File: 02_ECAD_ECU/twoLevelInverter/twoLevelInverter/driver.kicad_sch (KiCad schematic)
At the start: 30 parts, among them IC2 INA240A4DR, IC3 BTN8982TAAUMA1, IC4 INA240A4DR, IC5 BTN8982TAAUMA1, IC6 INA240A4DR, IC7 BTN8982TAAUMA1

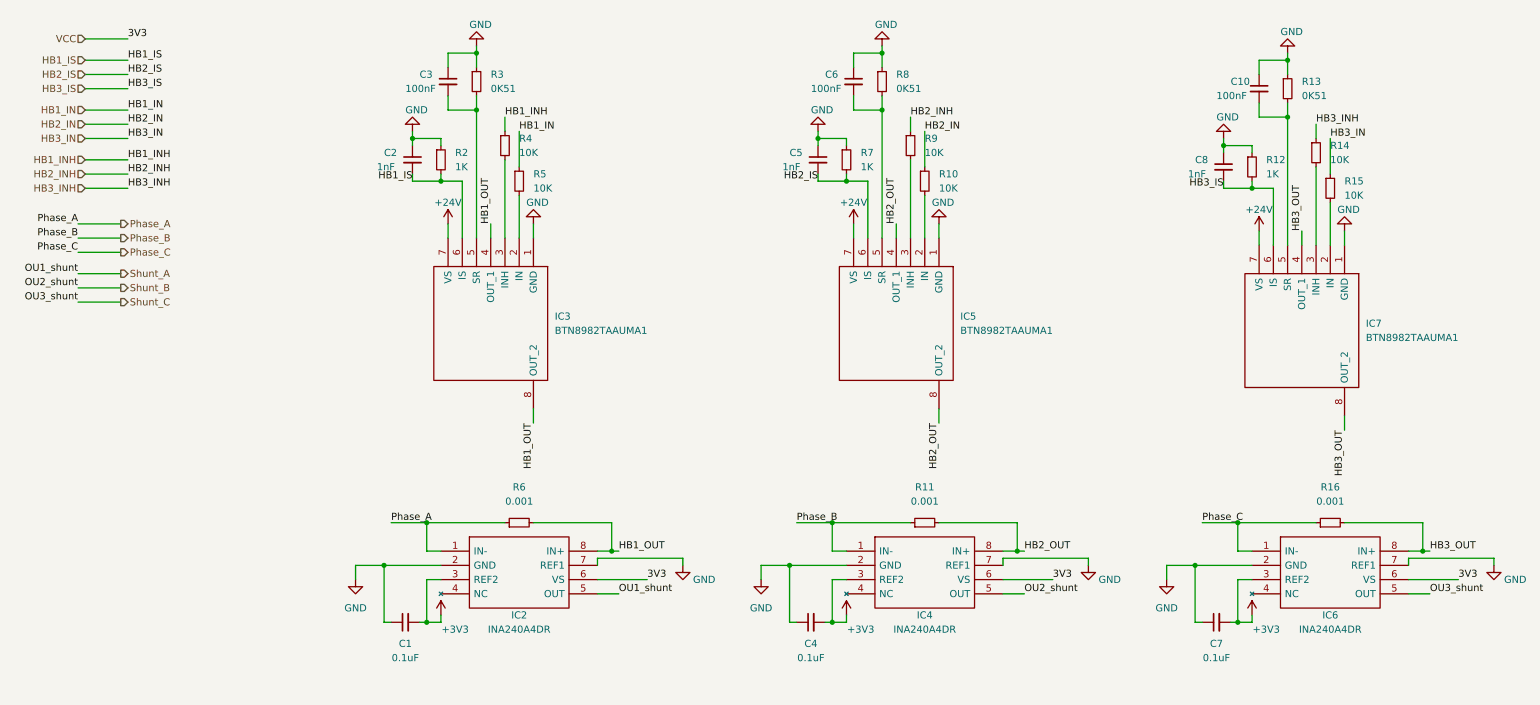
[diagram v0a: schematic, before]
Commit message: encoder, pwm, hall signals mapped
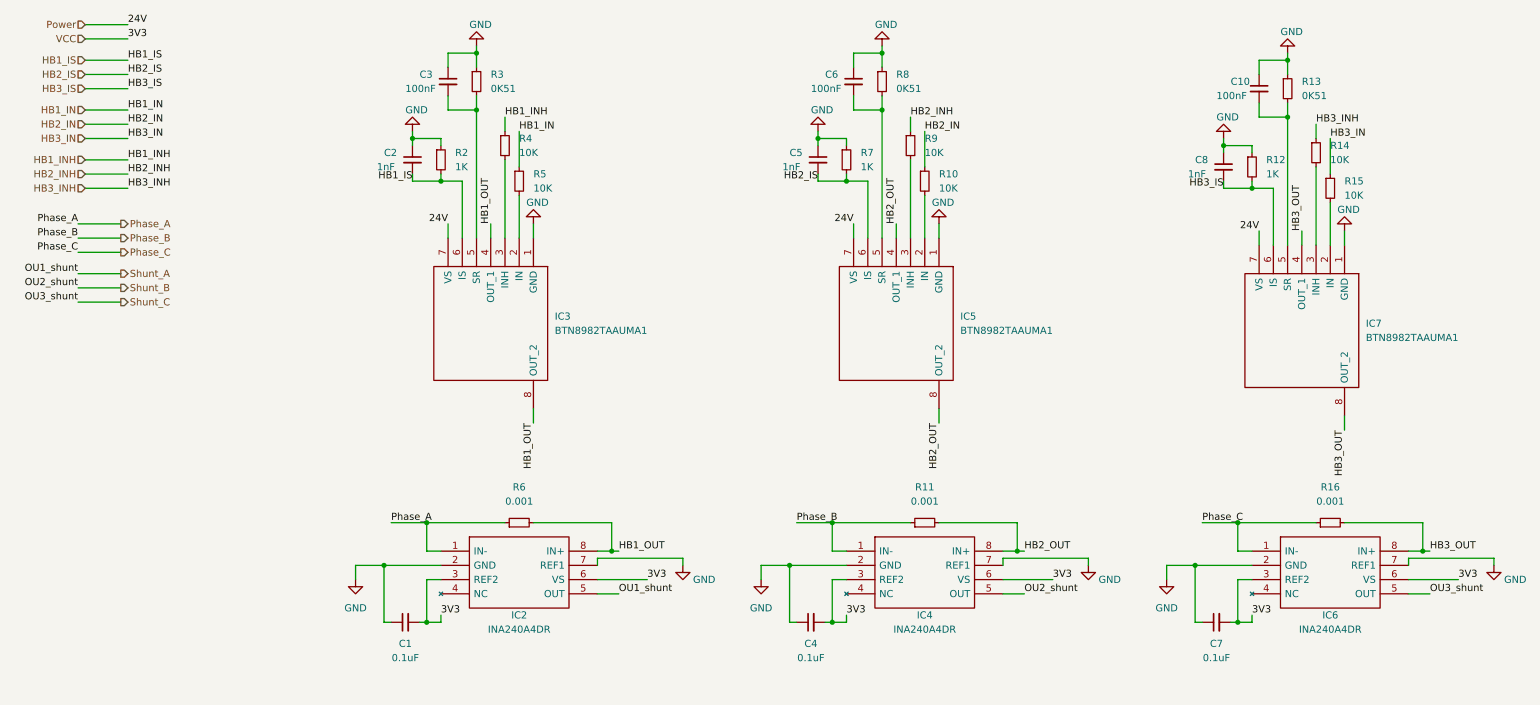
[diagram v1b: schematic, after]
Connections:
- net +3V3 is gone; now on net VCC: C1.2, C4.2, C7.2, IC2.3 (REF2), IC4.3 (REF2), IC6.3 (REF2)
- net +24V renamed Power
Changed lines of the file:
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@@
+    (stroke (width 0) (type default) (color 0 0 0 0))
+  )
+  (wire (pts (xy 25.4 17.78) (xy 33.02 17.78))
     (stroke (width 0) (type default) (color 0 0 0 0))
   )
@@
     (effects (font (size 1.27 1.27)) (justify left bottom))
   )
+  (label "24V" (at 234.95 54.61 180)
+    (effects (font (size 1.27 1.27)) (justify right bottom))
+  )
   (label "Phase_B" (at 152.4 106.68 0)
     (effects (font (size 1.27 1.27)) (justify left bottom))
@@
     (effects (font (size 1.27 1.27)) (justify left bottom))
   )
+  (label "3V3" (at 161.29 123.19 0)
+    (effects (font (size 1.27 1.27)) (justify left bottom))
+  )
   (label "HB2_OUT" (at 170.18 53.34 90)
     (effects (font (size 1.27 1.27)) (justify left bottom))
@@
     (effects (font (size 1.27 1.27)) (justify left bottom))
   )
+  (label "24V" (at 162.56 53.34 180)
+    (effects (font (size 1.27 1.27)) (justify right bottom))
+  )
   (label "HB1_IN" (at 102.87 36.83 0)
     (effects (font (size 1.27 1.27)) (justify left bottom))
   )
+  (label "24V" (at 90.17 53.34 180)
+    (effects (font (size 1.27 1.27)) (justify right bottom))
+  )
   (label "Phase_A" (at 80.01 106.68 0)
     (effects (font (size 1.27 1.27)) (justify left bottom))
@@
     (effects (font (size 1.27 1.27)) (justify left bottom))
   )
+  (label "3V3" (at 88.9 123.19 0)
+    (effects (font (size 1.27 1.27)) (justify left bottom))
+  )
+  (label "3V3" (at 233.68 123.19 0)
+    (effects (font (size 1.27 1.27)) (justify left bottom))
+  )
   (label "HB2_IS" (at 156.21 45.72 180)
     (effects (font (size 1.27 1.27)) (justify right bottom))
@@
   (label "HB1_IS" (at 83.82 45.72 180)
     (effects (font (size 1.27 1.27)) (justify right bottom))
+  )
+  (label "24V" (at 33.02 17.78 0)
+    (effects (font (size 1.27 1.27)) (justify left bottom))
   )
   (label "3V3" (at 270.51 116.84 0)
@@
   )
   (hierarchical_label "VCC" (shape input) (at 25.4 20.32 180)
+    (effects (font (size 1.27 1.27)) (justify right))
+  )
+  (hierarchical_label "Power" (shape input) (at 25.4 17.78 180)
     (effects (font (size 1.27 1.27)) (justify right))
   )
@@
     (pin "1")
   )
-  (symbol (lib_id "power:+3V3") (at 161.29 123.19 0) (unit 1)
-    (in_bom yes) (on_board yes)
-    (property "Reference" "#PWR0105" (id 0) (at 161.29 127 0)
-      (effects (font (size 1.27 1.27)) hide)
-    )
-    (property "Value" "+3V3" (id 1) (at 163.83 125.73 0))
-    (property "Footprint" "" (id 2) (at 161.29 123.19 0)
-      (effects (font (size 1.27 1.27)) hide)
-    )
-    (property "Datasheet" "" (id 3) (at 161.29 123.19 0)
-      (effects (font (size 1.27 1.27)) hide)
-    )
-    (pin "1")
-  )
   (symbol (lib_id "Device:R_Small") (at 233.68 43.18 0) (unit 1)
     (in_bom yes) (on_board yes) (fields_autoplaced)
@@
     (pin "2")
   )
-  (symbol (lib_id "power:+24V") (at 234.95 54.61 0) (unit 1)
-    (in_bom yes) (on_board yes)
-    (property "Reference" "#PWR0125" (id 0) (at 234.95 58.42 0)
-      (effects (font (size 1.27 1.27)) hide)
-    )
-    (property "Value" "+24V" (id 1) (at 234.95 50.8 0))
-    (property "Footprint" "" (id 2) (at 234.95 54.61 0)
-      (effects (font (size 1.27 1.27)) hide)
-    )
-    (property "Datasheet" "" (id 3) (at 234.95 54.61 0)
-      (effects (font (size 1.27 1.27)) hide)
-    )
-    (pin "1")
-  )
   (symbol (lib_id "CustomLib:BTN8982TAAUMA1") (at 250.19 57.15 270) (unit 1)
     (in_bom yes) (on_board yes) (fields_autoplaced)
@@
     (pin "2")
   )
-  (symbol (lib_id "power:+3V3") (at 233.68 123.19 0) (unit 1)
-    (in_bom yes) (on_board yes)
-    (property "Reference" "#PWR0117" (id 0) (at 233.68 127 0)
-      (effects (font (size 1.27 1.27)) hide)
-    )
-    (property "Value" "+3V3" (id 1) (at 236.22 125.73 0))
-    (property "Footprint" "" (id 2) (at 233.68 123.19 0)
-      (effects (font (size 1.27 1.27)) hide)
-    )
-    (property "Datasheet" "" (id 3) (at 233.68 123.19 0)
-      (effects (font (size 1.27 1.27)) hide)
-    )
-    (pin "1")
-  )
   (symbol (lib_id "CustomLib:INA240A4DR") (at 233.68 111.76 0) (unit 1)
     (in_bom yes) (on_board yes)
@@
     (pin "1")
   )
-  (symbol (lib_id "power:+3V3") (at 88.9 123.19 0) (unit 1)
-    (in_bom yes) (on_board yes)
-    (property "Reference" "#PWR0115" (id 0) (at 88.9 127 0)
-      (effects (font (size 1.27 1.27)) hide)
-    )
-    (property "Value" "+3V3" (id 1) (at 91.44 125.73 0))
-    (property "Footprint" "" (id 2) (at 88.9 123.19 0)
-      (effects (font (size 1.27 1.27)) hide)
-    )
-    (property "Datasheet" "" (id 3) (at 88.9 123.19 0)
-      (effects (font (size 1.27 1.27)) hide)
-    )
-    (pin "1")
-  )
   (symbol (lib_id "Device:C_Small") (at 227.33 124.46 90) (unit 1)
     (in_bom yes) (on_board yes)
@@
     (pin "1")
     (pin "2")
-  )
-  (symbol (lib_id "power:+24V") (at 162.56 53.34 0) (unit 1)
-    (in_bom yes) (on_board yes)
-    (property "Reference" "#PWR0124" (id 0) (at 162.56 57.15 0)
-      (effects (font (size 1.27 1.27)) hide)
-    )
-    (property "Value" "+24V" (id 1) (at 162.56 49.53 0))
-    (property "Footprint" "" (id 2) (at 162.56 53.34 0)
-      (effects (font (size 1.27 1.27)) hide)
-    )
-    (property "Datasheet" "" (id 3) (at 162.56 53.34 0)
-      (effects (font (size 1.27 1.27)) hide)
-    )
-    (pin "1")
   )
   (symbol (lib_id "CustomLib:INA240A4DR") (at 161.29 111.76 0) (unit 1)
@@
     (pin "2")
   )
-  (symbol (lib_id "power:+24V") (at 90.17 53.34 0) (unit 1)
-    (in_bom yes) (on_board yes)
-    (property "Reference" "#PWR0112" (id 0) (at 90.17 57.15 0)
-      (effects (font (size 1.27 1.27)) hide)
-    )
-    (property "Value" "+24V" (id 1) (at 90.17 49.53 0))
-    (property "Footprint" "" (id 2) (at 90.17 53.34 0)
-      (effects (font (size 1.27 1.27)) hide)
-    )
-    (property "Datasheet" "" (id 3) (at 90.17 53.34 0)
-      (effects (font (size 1.27 1.27)) hide)
-    )
-    (pin "1")
-  )
   (symbol (lib_id "Device:C_Small") (at 156.21 41.91 0) (unit 1)

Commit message: V1.0  not reviewed
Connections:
- net GND: now also C1.2, C4.2, C7.2, IC2.3 (REF2), IC2.4 (NC), IC4.3 (REF2), IC4.4 (NC), IC6.3 (REF2), IC6.4 (NC); no longer C1.1, C4.1, C7.1, IC2.7 (REF1), IC4.7 (REF1), IC6.7 (REF1)
- net HB1_OUT: no longer IC3.4 (OUT_1)
- net HB2_OUT: no longer IC5.4 (OUT_1)
- net HB3_OUT: no longer IC7.4 (OUT_1)
- net VCC: now also C1.1, C4.1, C7.1, IC2.7 (REF1), IC4.7 (REF1), IC6.7 (REF1); no longer C1.2, C4.2, C7.2, IC2.3 (REF2), IC4.3 (REF2), IC6.3 (REF2)
- no-connect marks 0 -> 3
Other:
- moved on the sheet: C1, C7, IC2, IC4, IC6, R11, R16, R6
